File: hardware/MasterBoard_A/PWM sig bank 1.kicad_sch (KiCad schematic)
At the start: 17 parts, among them U15 TLP155E, U16 TLP155E, U17 TLP155E, U3 TLP155E

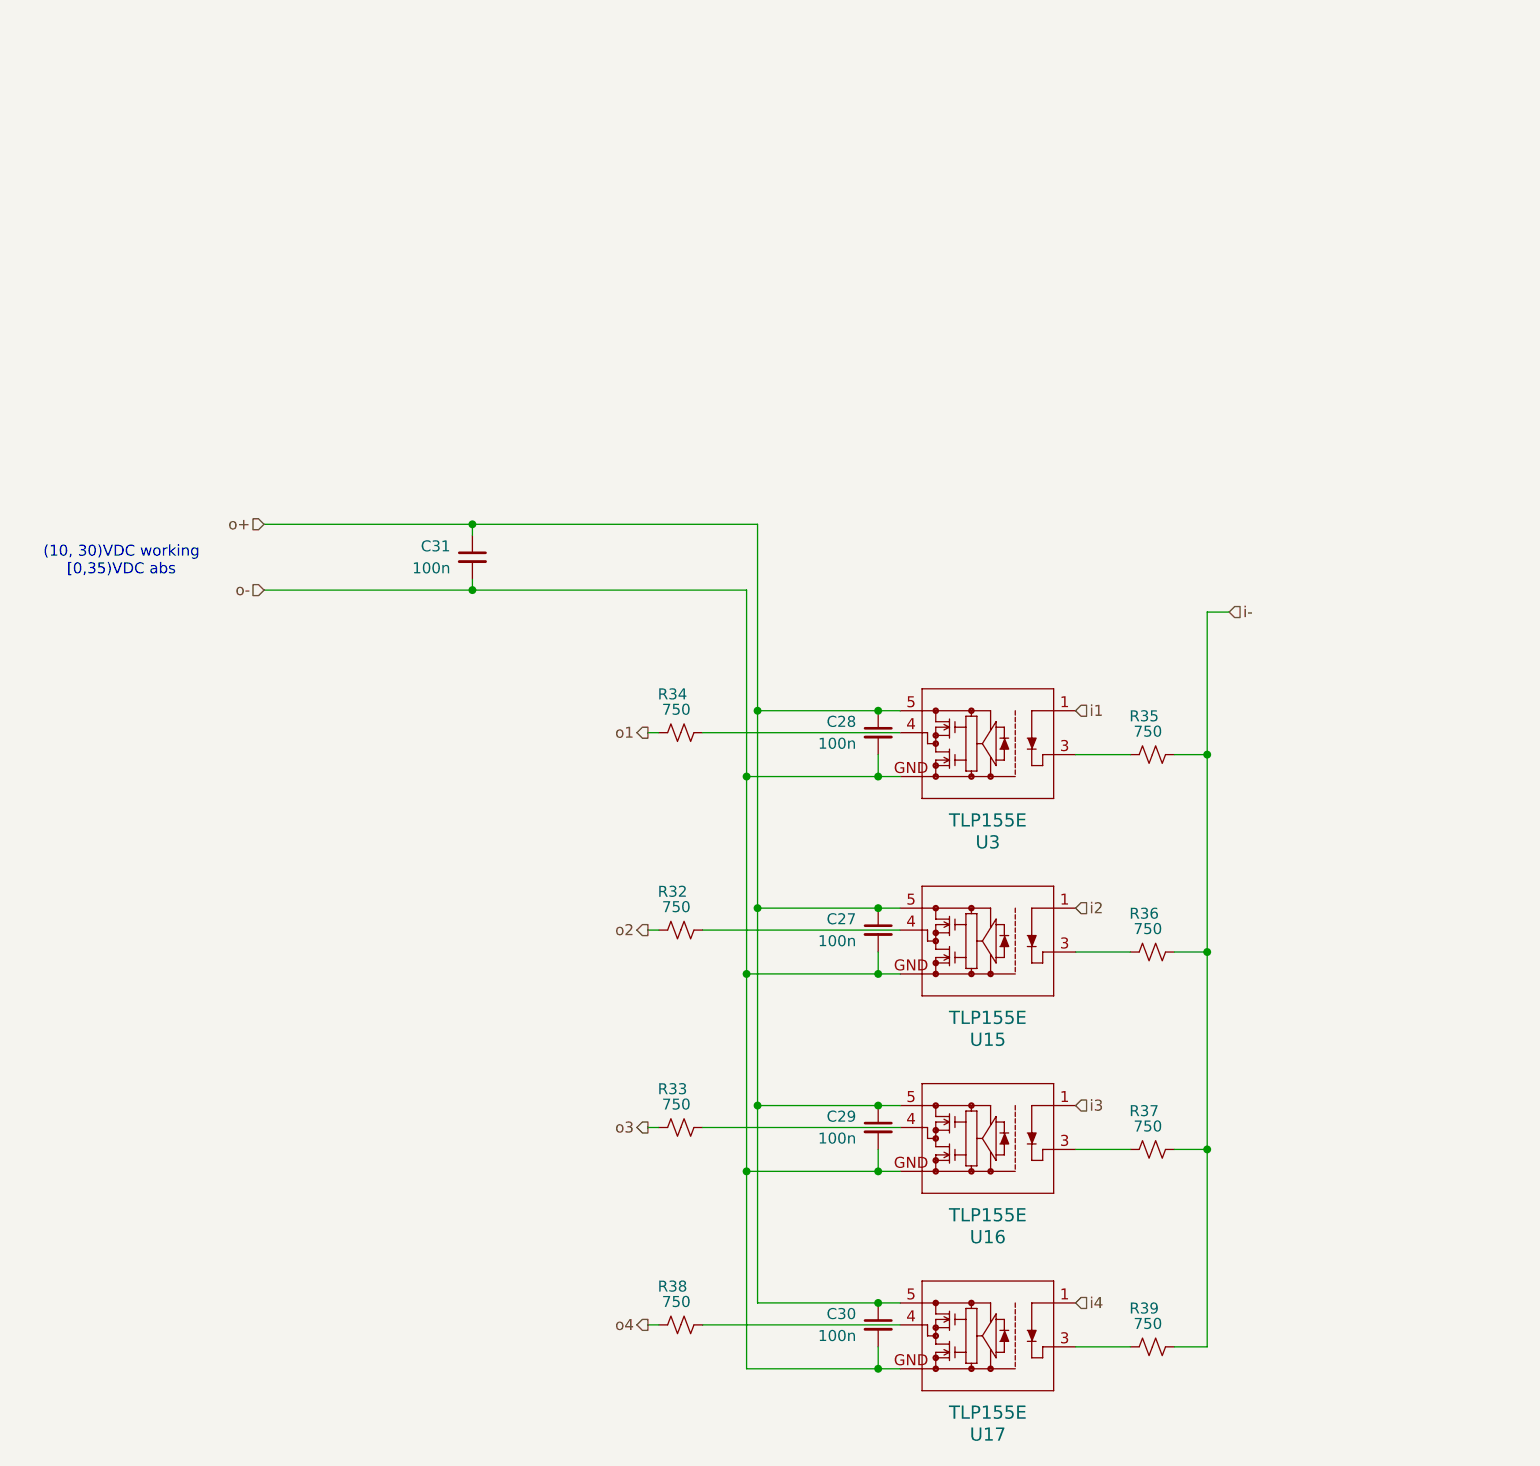
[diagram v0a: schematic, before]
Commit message: corrected HRLV IL couple
W5500 D:. idk bruh, looking like debug hell
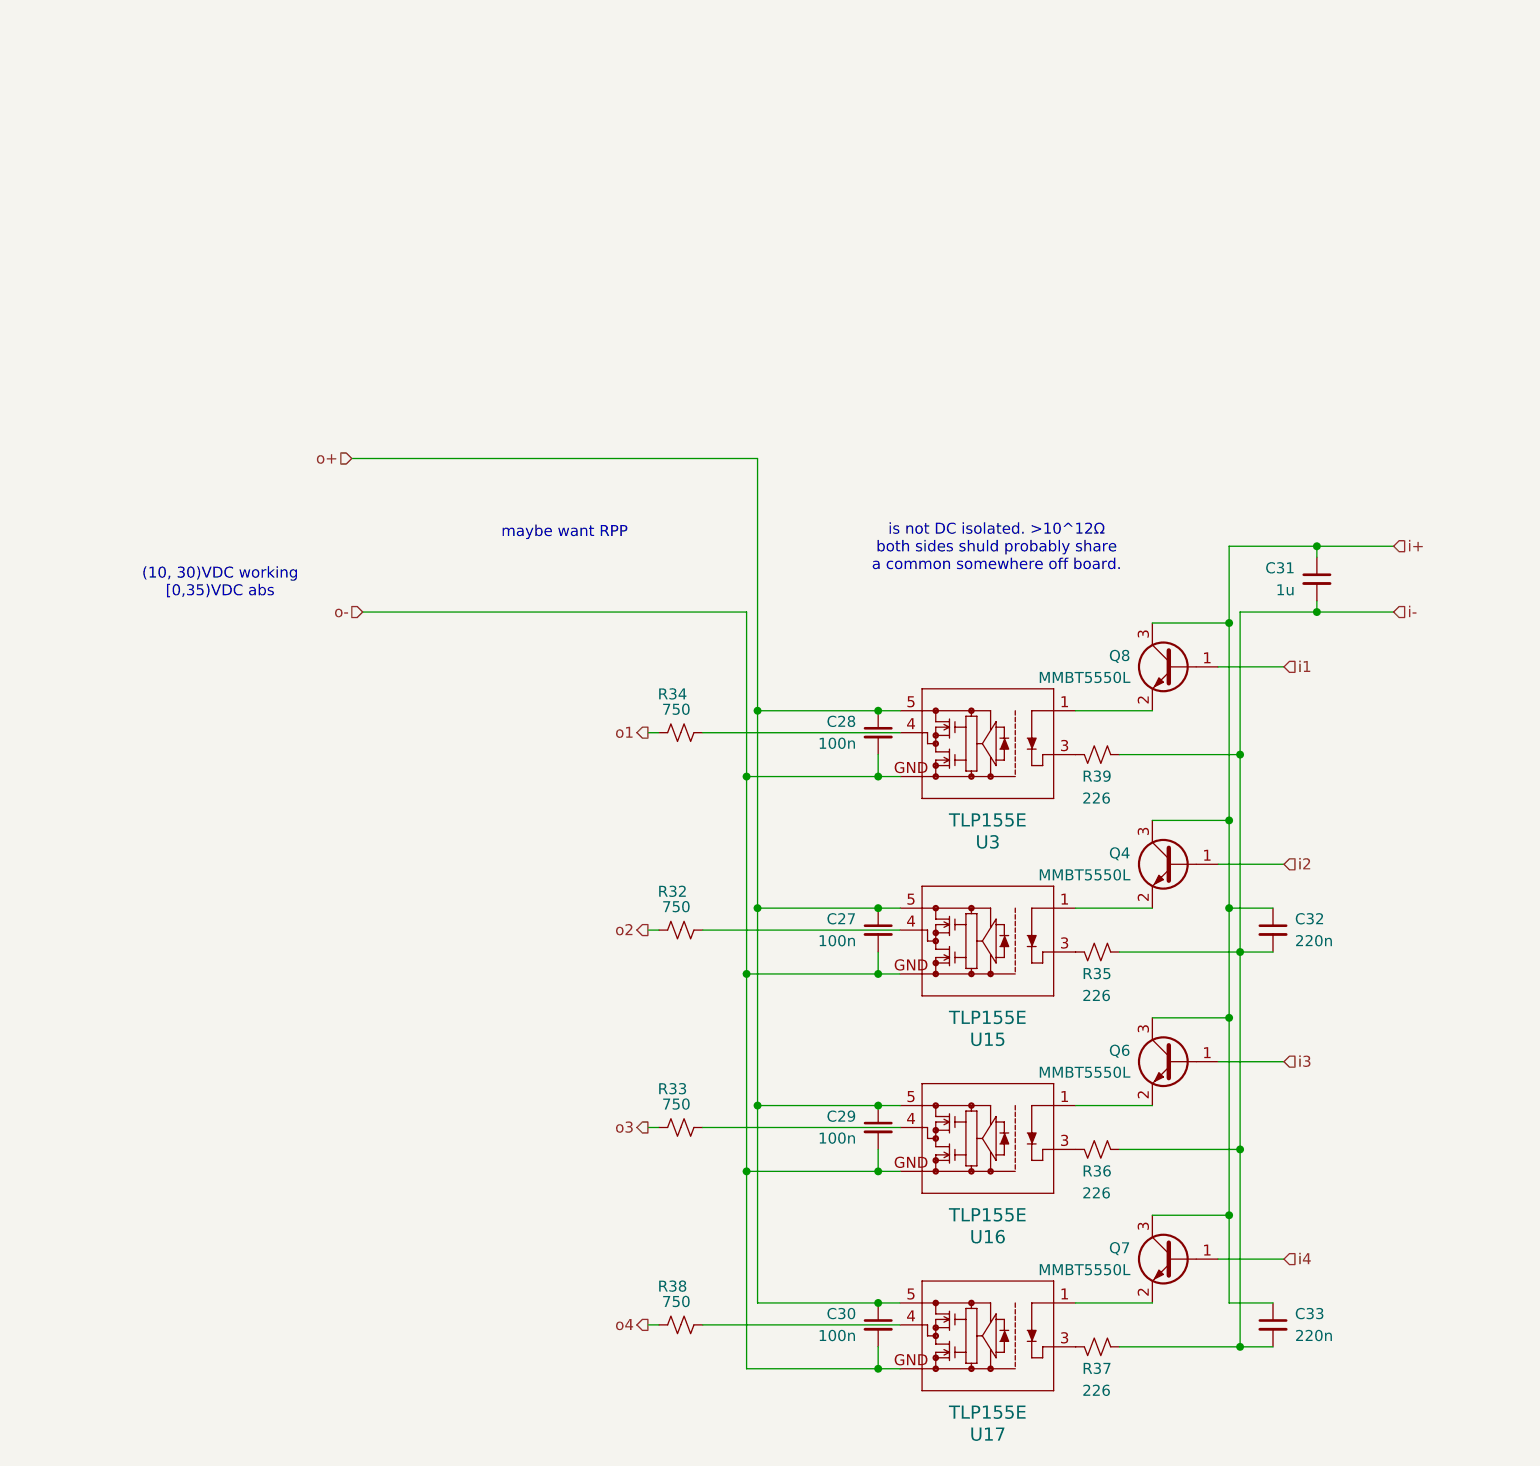
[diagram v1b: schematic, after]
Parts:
- added C32, C33: 220n, Capacitor_SMD:C_1206_3216Metric_Pad1.33x1.80mm_HandSolder, symbol Device:C_Small
- added Q4, Q6, Q7, Q8: MMBT5550L, Package_TO_SOT_SMD:SOT-23, symbol Transistor_BJT:MMBT5550L
- C31: value 100n -> 1u; mouser https://www.mouser.com/ProductDetail/Walsin/1206B104K251CT?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 -> https://www.mouser.com/ProductDetail/Samsung-Electro-Mechan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; specs 100nF, 250VDC, X7R, 10%, -55C, +125C -> 1uF, 100VDC, X7R, 10%, -55C, +125C; unit x10 0.042 -> 0.07
- R35, R36, R37, R39: value 750 -> 226; footprint Resistor_SMD:R_1206_3216Metric_Pad1.30x1.75mm_HandSolder -> Resistor_SMD:R_0805_2012Metric_Pad1.20x1.40mm_HandSolder; mouser https://www.mouser.com/ProductDetail/YAGEO/RC1206JR-13750RL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 -> https://www.mouser.com/ProductDetail/KOA-Speer/RK73H2BTTD22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; specs 750mOhm, 250mW, 5%, 100PPM, 200C, -55C, +155C -> 226Ohm, 250mW, 1%, 200V, -55C, +155C; unit x1 0.1 -> 0.10; unit x10 0.022 -> 0.023
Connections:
- net i-: now also C31.2, R35.2, R36.2, R37.2, R39.2, C32.2, C33.2; no longer R35.1, R36.1, R37.1, R39.1
- net i1: now also Q8.1 (B); no longer U3.1
- net i2: now also Q4.1 (B); no longer U15.1
- net i3: now also Q6.1 (B); no longer U16.1
- net i4: now also Q7.1 (B); no longer U17.1
- net o+: no longer C31.1
- net o-: no longer C31.2
- net at U15.3: now also R35.1; no longer R36.2
- net at U3.3: now also R39.1; no longer R35.2
- net at U16.3: now also R36.1; no longer R37.2
- net at U17.3: now also R37.1; no longer R39.2
- new net: Q4.2 (E), U15.1
- new net: Q6.2 (E), U16.1
- new net: Q8.2 (E), U3.1
- new net: Q7.2 (E), U17.1
- new net i+: C31.1, C32.1, C33.1, Q4.3 (C), Q6.3 (C), Q7.3 (C), Q8.3 (C)
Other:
- note added: "is not DC isolated. >10^12Ω both sides shuld probably share a common somewhere off board."
- note added: "maybe want RPP"

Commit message: some progress
w5500 maybe works? shuffled around some more stuff and what not
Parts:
- added C38: 1u, Capacitor_SMD:C_1206_3216Metric_Pad1.33x1.80mm_HandSolder, symbol Device:C_Small
- added C39: 220n, Capacitor_SMD:C_0805_2012Metric_Pad1.18x1.45mm_HandSolder, symbol Device:C_Small
- added D25: green, LED_SMD:LED_0805_2012Metric_Pad1.15x1.40mm_HandSolder, symbol Device:LED_Small
- added D28, D30, D32, D34: yellow, LED_SMD:LED_0805_2012Metric_Pad1.15x1.40mm_HandSolder, symbol Device:LED_Small
- added Q16, Q17: MMBT5550L, Package_TO_SOT_SMD:SOT-23, symbol Transistor_BJT:MMBT5550L
- added R106, R31, R41, R45, R50: 39k, Resistor_SMD:R_0805_2012Metric_Pad1.20x1.40mm_HandSolder, symbol Device:R_Small_US
- added R107: 226, Resistor_SMD:R_0805_2012Metric_Pad1.20x1.40mm_HandSolder, symbol Device:R_Small_US
- added R42: 3.32k, Resistor_SMD:R_0805_2012Metric_Pad1.20x1.40mm_HandSolder, symbol Device:R_Small_US
- added R43: 750, Resistor_SMD:R_1206_3216Metric_Pad1.30x1.75mm_HandSolder, symbol Device:R_Small_US
- added R44, R46: 97.6k, Resistor_SMD:R_0805_2012Metric_Pad1.20x1.40mm_HandSolder, symbol Device:R_Small_US
- added U20, U23: IPD70R, Package_TO_SOT_SMD:TO-252-2, symbol zzLocalLibrary:IPD70R
- added U21: LM74502, Package_TO_SOT_SMD:SOT-23-8_Handsoldering, symbol zzLocalLibrary:LM74502
- C32, C33: footprint Capacitor_SMD:C_1206_3216Metric_Pad1.33x1.80mm_HandSolder -> Capacitor_SMD:C_0805_2012Metric_Pad1.18x1.45mm_HandSolder; mouser https://www.mouser.com/ProductDetail/Samsung-Electro-Mechanics/CL31B224KBFNNNF?qs=sGAEpiMZZMsh%252B1woXyUXj7iNKXiFkBmw7C%252BUlKpuDJ8%3D -> https://www.mouser.com/ProductDetail/Samsung-Electro-Mechanics/CL21B224KCFSFNE?qs=664zcAxDQ0l4Y1eUk6Zc1g%3D%3D; specs 50VDC, X7R, 10%, -55C, +125C, 220nF -> 100VDC, X7R, 10%, -55C, +125C, 220nF
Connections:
- net i-: now also R31.1, R41.1, R45.1, R50.1
- net i1: now also D28.2 (A), R41.2; no longer Q8.1 (B)
- net i2: now also D30.2 (A), R31.2; no longer Q4.1 (B)
- net i3: now also D32.2 (A), R45.2; no longer Q6.1 (B)
- net i4: now also D34.2 (A), R50.2; no longer Q7.1 (B)
- net o+: now also C39.1, R44.2, R46.2, U20.2 (D), U21.5 (VS); no longer C27.1, C28.1, C29.1, C30.1, U15.5, U16.5, U17.5, U3.5
- net o-: now also C38.1, R43.1, U21.2 (GND)
- new net: C27.1, C28.1, C29.1, C30.1, C38.2, D25.2 (A), R106.2, U15.5, U16.5, U17.5, U23.2 (D), U3.5
- new net: R42.2, R44.1, U21.7 (OV)
- new net: R46.1, U21.1 (EN/UVLO)
- new net: D25.1 (K), Q17.3 (C)
- new net: Q16.1 (B), Q17.2 (E), R107.1
- new net: Q16.2 (E), R107.2
- new net: Q16.3 (C), Q17.1 (B), R106.1
- new net: U20.1 (G), U21.6 (GATE), U23.1 (G)
- new net: U20.3 (S), U21.8 (SRC), U23.3 (S)
- new net: D34.1 (K), Q7.1 (B)
- new net: D30.1 (K), Q4.1 (B)
- new net: R42.1, R43.2
- new net: C39.2, U21.4 (VCAP)
- new net: D28.1 (K), Q8.1 (B)
- new net: D32.1 (K), Q6.1 (B)
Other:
- note added: "(6, 30)V"
- note added: "OV, RPP"
- note removed: "(10, 30)VDC working [0,35)VDC abs"
- note removed: "maybe want RPP"
- moved on the sheet: C27, C28, C29, C30, C31, C32, C33, Q4, Q6, Q7, Q8, R32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
